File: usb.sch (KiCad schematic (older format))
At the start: 33 parts, among them IC1 EP4CE10F17, P1 USB_A, U23 FT313HL-LQFP64-0.5, U25 TPS2024D, Y2 12MHz

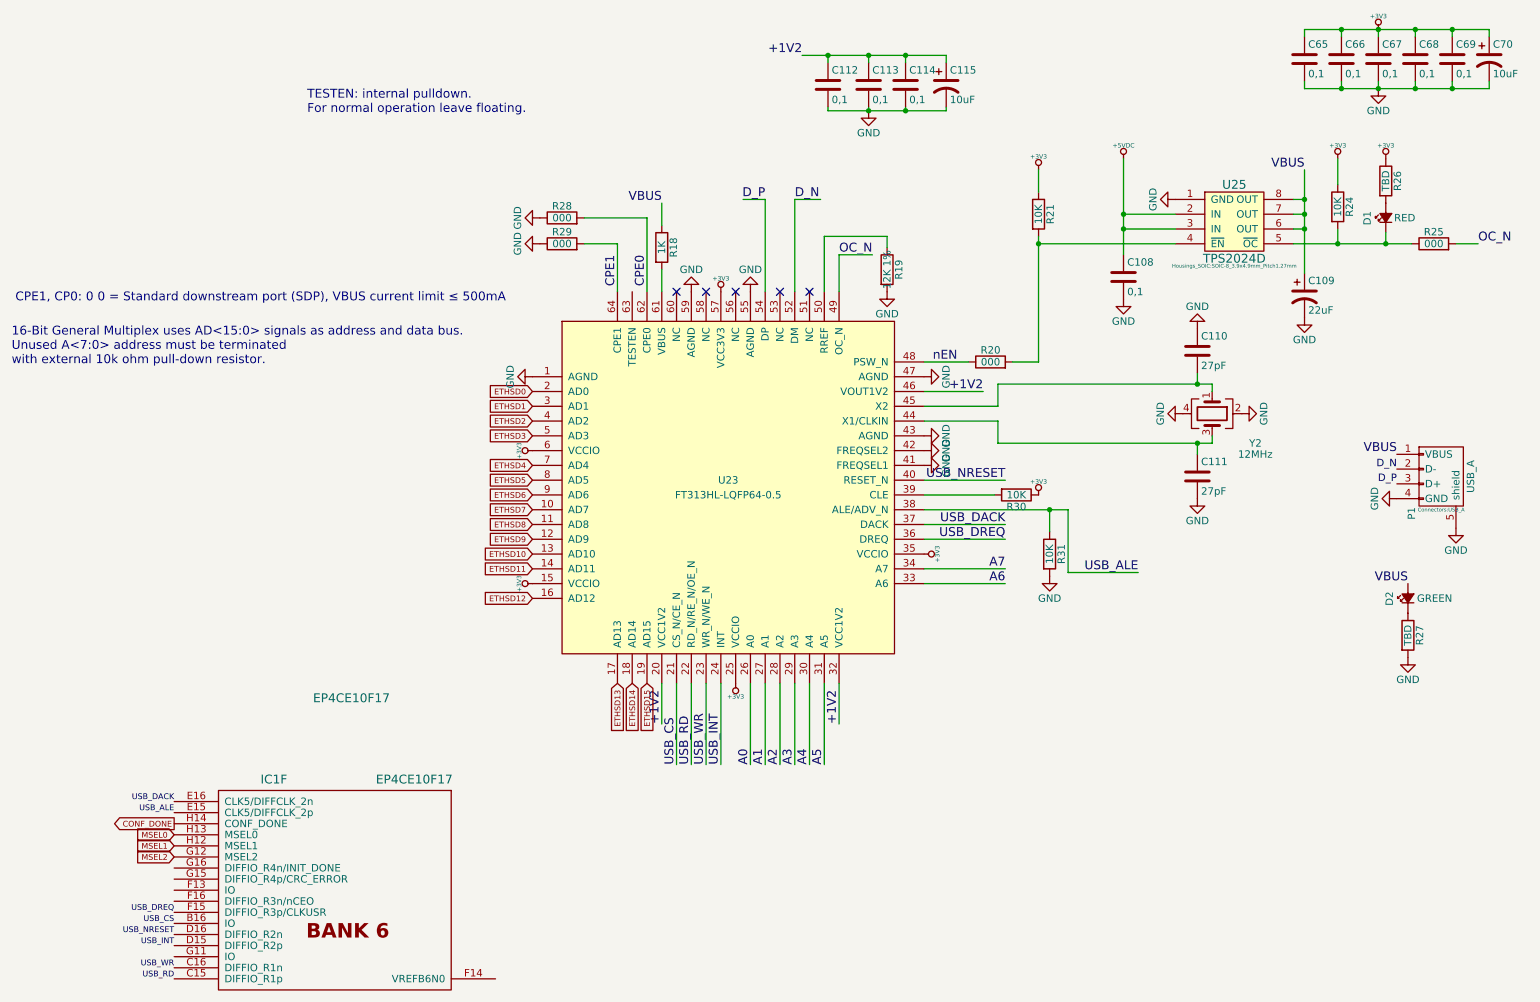
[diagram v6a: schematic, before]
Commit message: FT313 unused A0..A7 lines tied to GND
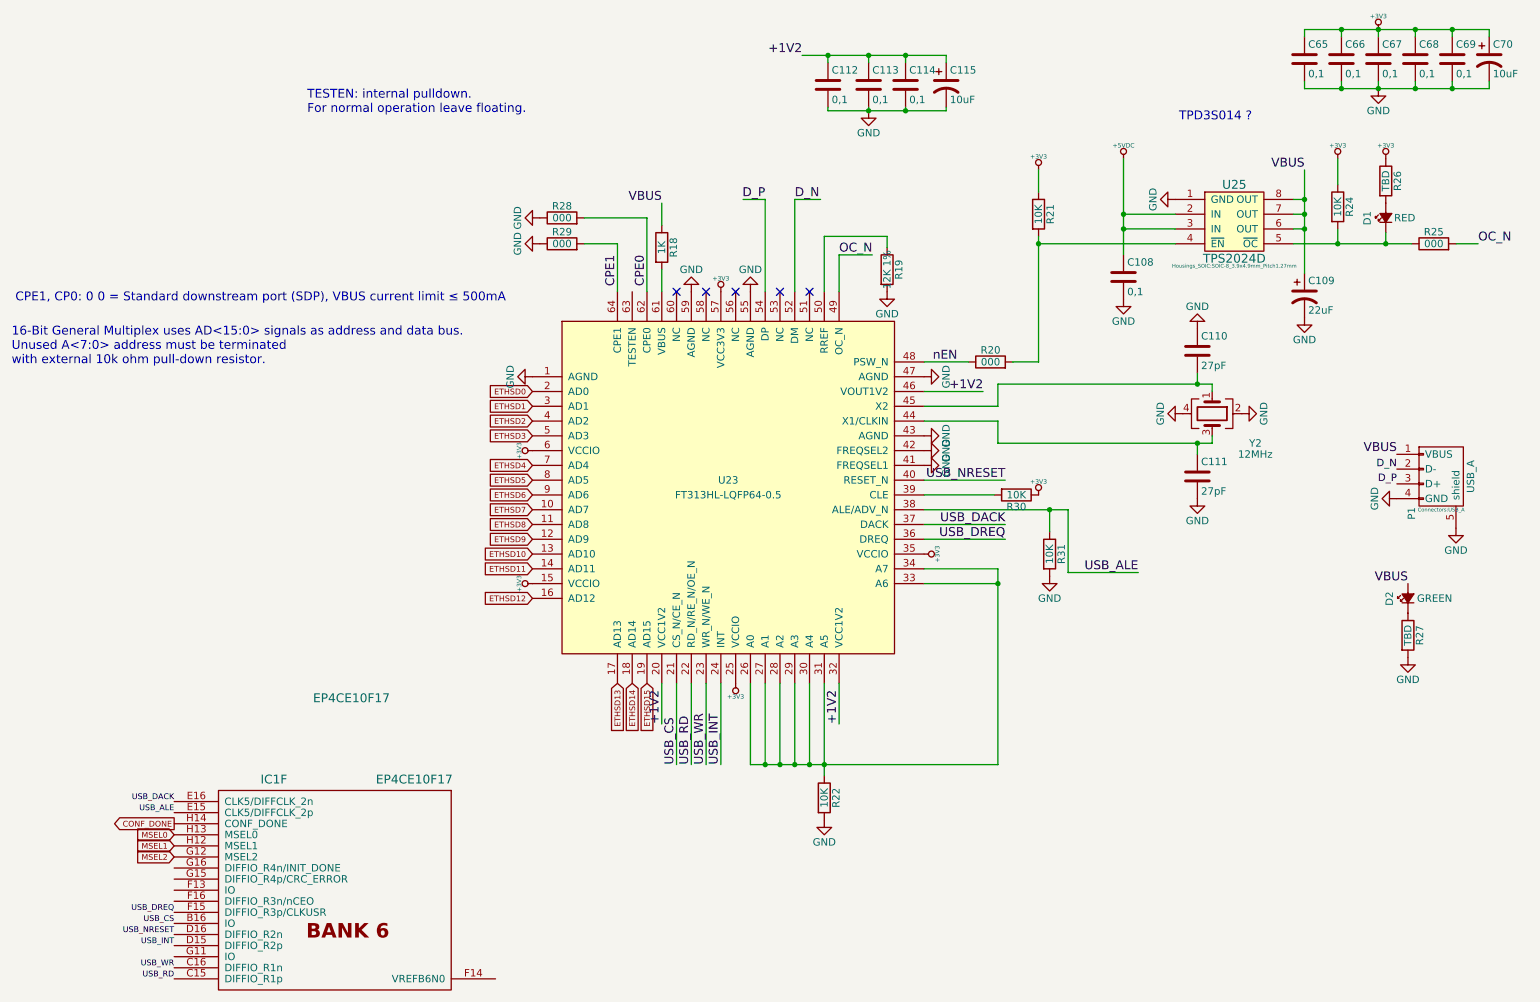
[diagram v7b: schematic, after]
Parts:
- added R22: 10K, Resistors_SMD:R_0603, symbol R
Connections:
- net A1 is gone; now on an unnamed net: U23.27 (A1)
- net A2 is gone; now on an unnamed net: U23.28 (A2)
- net A3 is gone; now on an unnamed net: U23.29 (A3)
- net A4 is gone; now on an unnamed net: U23.30 (A4)
- net A5 is gone; now on an unnamed net: U23.31 (A5)
- net A6 is gone; now on an unnamed net: U23.33 (A6)
- net A7 is gone; now on an unnamed net: U23.34 (A7)
- net GND: now also R22.2
- net A0: no longer names the net of U23.26 (A0)
- net A0: now also R22.1
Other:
- note added: "TPD3S014 ?"
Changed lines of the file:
@@
 NoConn ~ 5325 2450
 $Comp
-L GND #PWR0141
+L GND #PWR141
 U 1 1 587F93F7
 P 4350 3025
-F 0 "#PWR0141" H 4350 2775 50  0001 C CNN
+F 0 "#PWR141" H 4350 2775 50  0001 C CNN
 F 1 "GND" H 4350 2875 50  0000 C CNN
 F 2 "" H 4350 3025 50  0000 C CNN
@@
 $EndComp
 $Comp
-L GND #PWR0142
+L GND #PWR154
 U 1 1 587F942A
 P 7000 3425
-F 0 "#PWR0142" H 7000 3175 50  0001 C CNN
+F 0 "#PWR154" H 7000 3175 50  0001 C CNN
 F 1 "GND" H 7000 3275 50  0000 C CNN
 F 2 "" H 7000 3425 50  0000 C CNN
@@
 $EndComp
 $Comp
-L GND #PWR0143
+L GND #PWR153
 U 1 1 587F944F
 P 7000 3025
-F 0 "#PWR0143" H 7000 2775 50  0001 C CNN
+F 0 "#PWR153" H 7000 2775 50  0001 C CNN
 F 1 "GND" H 7000 2875 50  0000 C CNN
 F 2 "" H 7000 3025 50  0000 C CNN
@@
 $EndComp
 $Comp
-L GND #PWR0144
+L GND #PWR149
 U 1 1 587F9489
 P 5825 2450
-F 0 "#PWR0144" H 5825 2200 50  0001 C CNN
+F 0 "#PWR149" H 5825 2200 50  0001 C CNN
 F 1 "GND" H 5825 2300 50  0000 C CNN
 F 2 "" H 5825 2450 50  0000 C CNN
@@
 $EndComp
 $Comp
-L GND #PWR0145
+L GND #PWR146
 U 1 1 587F9497
 P 5425 2450
-F 0 "#PWR0145" H 5425 2200 50  0001 C CNN
+F 0 "#PWR146" H 5425 2200 50  0001 C CNN
 F 1 "GND" H 5425 2300 50  0000 C CNN
 F 2 "" H 5425 2450 50  0000 C CNN
@@
 $EndComp
 $Comp
-L +3V3 #PWR0146
+L +3V3 #PWR170
 U 1 1 587FA4A0
 P 10075 675
-F 0 "#PWR0146" H 10175 725 20  0001 C CNN
+F 0 "#PWR170" H 10175 725 20  0001 C CNN
 F 1 "+3V3" H 10075 765 30  0000 C CNN
 F 2 "" H 10075 675 60  0000 C CNN
@@
 $EndComp
 $Comp
-L GND #PWR0147
+L GND #PWR171
 U 1 1 587FA6CC
 P 10075 1075
-F 0 "#PWR0147" H 10075 825 50  0001 C CNN
+F 0 "#PWR171" H 10075 825 50  0001 C CNN
 F 1 "GND" H 10075 925 50  0000 C CNN
 F 2 "" H 10075 1075 50  0000 C CNN
@@
 $EndComp
 $Comp
-L +3V3 #PWR0148
+L +3V3 #PWR142
 U 1 1 587FB090
 P 4350 3525
-F 0 "#PWR0148" H 4450 3575 20  0001 C CNN
+F 0 "#PWR142" H 4450 3575 20  0001 C CNN
 F 1 "+3V3" H 4350 3615 30  0000 C CNN
 F 2 "" H 4350 3525 60  0000 C CNN
@@
 $EndComp
 $Comp
-L +3V3 #PWR0149
+L +3V3 #PWR148
 U 1 1 587FB177
 P 5725 5100
-F 0 "#PWR0149" H 5825 5150 20  0001 C CNN
+F 0 "#PWR148" H 5825 5150 20  0001 C CNN
 F 1 "+3V3" H 5725 5190 30  0000 C CNN
 F 2 "" H 5725 5100 60  0000 C CNN
@@
 $EndComp
 $Comp
-L +3V3 #PWR0150
+L +3V3 #PWR157
 U 1 1 587FB222
 P 7000 4225
-F 0 "#PWR0150" H 7100 4275 20  0001 C CNN
+F 0 "#PWR157" H 7100 4275 20  0001 C CNN
 F 1 "+3V3" H 7000 4315 30  0000 C CNN
 F 2 "" H 7000 4225 60  0000 C CNN
@@
 $EndComp
 $Comp
-L +3V3 #PWR0151
+L +3V3 #PWR143
 U 1 1 587FB43F
 P 4350 4425
-F 0 "#PWR0151" H 4450 4475 20  0001 C CNN
+F 0 "#PWR143" H 4450 4475 20  0001 C CNN
 F 1 "+3V3" H 4350 4515 30  0000 C CNN
 F 2 "" H 4350 4425 60  0000 C CNN
@@
 	0    -1   -1   0
 $EndComp
-Text Label 5825 5650 1    60   ~ 0
-A0
-Text Label 5925 5650 1    60   ~ 0
-A1
-Text Label 6025 5650 1    60   ~ 0
-A2
-Text Label 6125 5650 1    60   ~ 0
-A3
-Text Label 6225 5650 1    60   ~ 0
-A4
-Text Label 6325 5650 1    60   ~ 0
-A5
-Text Label 7550 4425 2    60   ~ 0
-A6
-Text Label 7550 4325 2    60   ~ 0
-A7
 Text Label 5225 5375 1    60   ~ 0
 +1V2
@@
 +1V2
 $Comp
-L +3V3 #PWR0152
+L +3V3 #PWR147
 U 1 1 587FFC16
 P 5625 2450
-F 0 "#PWR0152" H 5725 2500 20  0001 C CNN
+F 0 "#PWR147" H 5725 2500 20  0001 C CNN
 F 1 "+3V3" H 5625 2540 30  0000 C CNN
 F 2 "" H 5625 2450 60  0000 C CNN
@@
 $EndComp
 $Comp
-L GND #PWR0153
+L GND #PWR152
 U 1 1 588FBF68
 P 6750 2450
-F 0 "#PWR0153" H 6750 2200 50  0001 C CNN
+F 0 "#PWR152" H 6750 2200 50  0001 C CNN
 F 1 "GND" H 6750 2300 50  0000 C CNN
 F 2 "" H 6750 2450 50  0000 C CNN
@@
 D_P
 $Comp
-L GND #PWR0154
+L GND #PWR173
 U 1 1 588FD418
 P 10200 3850
-F 0 "#PWR0154" H 10200 3600 50  0001 C CNN
+F 0 "#PWR173" H 10200 3600 50  0001 C CNN
 F 1 "GND" H 10200 3700 50  0000 C CNN
 F 2 "" H 10200 3850 50  0000 C CNN
@@
 $EndComp
 $Comp
-L GND #PWR0155
+L GND #PWR175
 U 1 1 588FDBE9
 P 10600 4050
-F 0 "#PWR0155" H 10600 3800 50  0001 C CNN
+F 0 "#PWR175" H 10600 3800 50  0001 C CNN
 F 1 "GND" H 10600 3900 50  0000 C CNN
 F 2 "" H 10600 4050 50  0000 C CNN
@@
 $EndComp
 $Comp
-L GND #PWR0156
+L GND #PWR163
 U 1 1 5890EDC6
 P 8700 1825
-F 0 "#PWR0156" H 8700 1575 50  0001 C CNN
+F 0 "#PWR163" H 8700 1575 50  0001 C CNN
 F 1 "GND" H 8700 1675 50  0000 C CNN
 F 2 "" H 8700 1825 50  0000 C CNN
@@
 $EndComp
 $Comp
-L GND #PWR0157
+L GND #PWR162
 U 1 1 5890F077
 P 8350 2500
-F 0 "#PWR0157" H 8350 2250 50  0001 C CNN
+F 0 "#PWR162" H 8350 2250 50  0001 C CNN
 F 1 "GND" H 8350 2350 50  0000 C CNN
 F 2 "" H 8350 2500 50  0000 C CNN
@@
 $EndComp
 $Comp
-L +3V3 #PWR0158
+L +3V3 #PWR158
 U 1 1 589100DF
 P 7775 1625
-F 0 "#PWR0158" H 7875 1675 20  0001 C CNN
+F 0 "#PWR158" H 7875 1675 20  0001 C CNN
 F 1 "+3V3" H 7775 1715 30  0000 C CNN
 F 2 "" H 7775 1625 60  0000 C CNN
@@
 $EndComp
 $Comp
-L +5VDC #PWR0159
+L +5VDC #PWR161
 U 1 1 58911317
 P 8350 1550
-F 0 "#PWR0159" H 8450 1600 20  0001 C CNN
+F 0 "#PWR161" H 8450 1600 20  0001 C CNN
 F 1 "+5VDC" H 8350 1640 30  0000 C CNN
 F 2 "" H 8350 1550 60  0000 C CNN
@@
 	6225 5100 6225 5650
 Wire Wire Line
-	6325 5100 6325 5650
-Wire Wire Line
-	7000 4425 7550 4425
-Wire Wire Line
-	7000 4325 7550 4325
+	6325 5100 6325 5725
 Wire Wire Line
 	5225 5100 5225 5375
@@
 	7500 3475 8950 3475
 $Comp
-L GND #PWR0160
+L GND #PWR155
 U 1 1 58918521
 P 7000 3525
-F 0 "#PWR0160" H 7000 3275 50  0001 C CNN
+F 0 "#PWR155" H 7000 3275 50  0001 C CNN
 F 1 "GND" H 7000 3375 50  0000 C CNN
 F 2 "" H 7000 3525 50  0000 C CNN
@@
 $EndComp
 $Comp
-L +3V3 #PWR0162
+L +3V3 #PWR169
 U 1 1 58919A0E
 P 9800 1550
-F 0 "#PWR0162" H 9900 1600 20  0001 C CNN
+F 0 "#PWR169" H 9900 1600 20  0001 C CNN
 F 1 "+3V3" H 9800 1640 30  0000 C CNN
 F 2 "" H 9800 1550 60  0000 C CNN
@@
 $EndComp
 $Comp
-L GND #PWR0163
+L GND #PWR168
 U 1 1 5891AE93
 P 9575 2625
-F 0 "#PWR0163" H 9575 2375 50  0001 C CNN
+F 0 "#PWR168" H 9575 2375 50  0001 C CNN
 F 1 "GND" H 9575 2475 50  0000 C CNN
 F 2 "" H 9575 2625 50  0000 C CNN
@@
 $EndComp
 $Comp
-L GND #PWR0164
+L GND #PWR164
 U 1 1 5891C617
 P 8750 3275
-F 0 "#PWR0164" H 8750 3025 50  0001 C CNN
+F 0 "#PWR164" H 8750 3025 50  0001 C CNN
 F 1 "GND" H 8750 3125 50  0000 C CNN
 F 2 "" H 8750 3275 50  0000 C CNN
@@
 $EndComp
 $Comp
-L GND #PWR0165
+L GND #PWR167
 U 1 1 5891C65E
 P 9150 3275
-F 0 "#PWR0165" H 9150 3025 50  0001 C CNN
+F 0 "#PWR167" H 9150 3025 50  0001 C CNN
 F 1 "GND" H 9150 3125 50  0000 C CNN
 F 2 "" H 9150 3275 50  0000 C CNN
@@
 Connection ~ 8850 3075
 $Comp
-L GND #PWR0166
+L GND #PWR166
 U 1 1 5891DDB7
 P 8850 3850
-F 0 "#PWR0166" H 8850 3600 50  0001 C CNN
+F 0 "#PWR166" H 8850 3600 50  0001 C CNN
 F 1 "GND" H 8850 3700 50  0000 C CNN
 F 2 "" H 8850 3850 50  0000 C CNN
@@
 $EndComp
 $Comp
-L GND #PWR0167
+L GND #PWR165
 U 1 1 5891DE04
 P 8850 2700
-F 0 "#PWR0167" H 8850 2450 50  0001 C CNN
+F 0 "#PWR165" H 8850 2450 50  0001 C CNN
 F 1 "GND" H 8850 2550 50  0000 C CNN
 F 2 "" H 8850 2700 50  0000 C CNN
@@
 Connection ~ 6875 1225
 $Comp
-L GND #PWR0168
+L GND #PWR151
 U 1 1 58A7680E
 P 6625 1225
-F 0 "#PWR0168" H 6625 975 50  0001 C CNN
+F 0 "#PWR151" H 6625 975 50  0001 C CNN
 F 1 "GND" H 6625 1075 50  0000 C CNN
 F 2 "" H 6625 1225 50  0000 C CNN
@@
 $EndComp
 $Comp
-L GND #PWR0169
+L GND #PWR174
 U 1 1 5895CD67
 P 10275 4925
-F 0 "#PWR0169" H 10275 4675 50  0001 C CNN
+F 0 "#PWR174" H 10275 4675 50  0001 C CNN
 F 1 "GND" H 10275 4775 50  0000 C CNN
 F 2 "" H 10275 4925 50  0000 C CNN
@@
 $EndComp
 $Comp
-L +3V3 #PWR0170
+L +3V3 #PWR172
 U 1 1 5895DF10
 P 10125 1550
-F 0 "#PWR0170" H 10225 1600 20  0001 C CNN
+F 0 "#PWR172" H 10225 1600 20  0001 C CNN
 F 1 "+3V3" H 10125 1640 30  0000 C CNN
 F 2 "" H 10125 1550 60  0000 C CNN
@@
 $EndComp
 $Comp
-L GND #PWR0171
+L GND #PWR144
 U 1 1 5897A8C7
 P 4400 1950
-F 0 "#PWR0171" H 4400 1700 50  0001 C CNN
+F 0 "#PWR144" H 4400 1700 50  0001 C CNN
 F 1 "GND" H 4400 1800 50  0000 C CNN
 F 2 "" H 4400 1950 50  0000 C CNN
@@
 $EndComp
 $Comp
-L GND #PWR0172
+L GND #PWR145
 U 1 1 5897A935
 P 4400 2125
-F 0 "#PWR0172" H 4400 1875 50  0001 C CNN
+F 0 "#PWR145" H 4400 1875 50  0001 C CNN
 F 1 "GND" H 4400 1975 50  0000 C CNN
 F 2 "" H 4400 2125 50  0000 C CNN
@@
 $EndComp
 $Comp
-L +3V3 #PWR0173
+L +3V3 #PWR159
 U 1 1 5898F68C
 P 7775 3825
-F 0 "#PWR0173" H 7875 3875 20  0001 C CNN
+F 0 "#PWR159" H 7875 3875 20  0001 C CNN
 F 1 "+3V3" H 7775 3915 30  0000 C CNN
 F 2 "" H 7775 3825 60  0000 C CNN
@@
 $EndComp
 $Comp
-L GND #PWR0174
+L GND #PWR160
 U 1 1 589900C4
 P 7850 4375
-F 0 "#PWR0174" H 7850 4125 50  0001 C CNN
+F 0 "#PWR160" H 7850 4125 50  0001 C CNN
 F 1 "GND" H 7850 4225 50  0000 C CNN
 F 2 "" H 7850 4375 50  0000 C CNN
@@
 USB_ALE
 $Comp
-L GND #PWR?
+L GND #PWR156
 U 1 1 5898F13F
 P 7000 3625
-F 0 "#PWR?" H 7000 3375 50  0001 C CNN
+F 0 "#PWR156" H 7000 3375 50  0001 C CNN
 F 1 "GND" H 7000 3475 50  0000 C CNN
 F 2 "" H 7000 3625 50  0000 C CNN
@@
 	0    -1   -1   0
 $EndComp
+Text Notes 8725 1300 0    60   ~ 0
+TPD3S014 ?
+Wire Wire Line
+	5825 5650 7500 5650
+Connection ~ 6225 5650
+Connection ~ 6125 5650
+Connection ~ 6025 5650
+Connection ~ 5925 5650
+$Comp
+L R R22
+U 1 1 58991820
+P 6325 5875
+F 0 "R22" V 6405 5875 50  0000 C CNN
+F 1 "10K" V 6325 5875 50  0000 C CNN
+F 2 "Resistors_SMD:R_0603" V 6255 5875 50  0001 C CNN
+F 3 "" H 6325 5875 50  0000 C CNN
+	1    6325 5875
+	1    0    0    -1
+$EndComp
+$Comp
+L GND #PWR150
+U 1 1 58991AA6
+P 6325 6025
+F 0 "#PWR150" H 6325 5775 50  0001 C CNN
+F 1 "GND" H 6325 5875 50  0000 C CNN
+F 2 "" H 6325 6025 50  0000 C CNN
+F 3 "" H 6325 6025 50  0000 C CNN
+	1    6325 6025
+	1    0    0    -1
+$EndComp
+Wire Wire Line
+	7500 5650 7500 4325
+Connection ~ 6325 5650
+Connection ~ 7500 4425
+Wire Wire Line
+	7500 4325 7000 4325
+Wire Wire Line
+	7000 4425 7500 4425
 $EndSCHEMATC
